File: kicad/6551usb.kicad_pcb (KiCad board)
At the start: 2 copper layers, 98.6 x 151.8 mm, 42 parts, among them J1 Conn_01x03_Male, P1 DLP-USB245R, SW1 SW_DIP_x06, U1 74LS04, U10 74LS74, U11 74LS86, U12 74LS33, U13 74LS273, U14 74LS374, U15 74LS244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

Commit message: Updated to 1.06
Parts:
- removed R4: 4.7k, Resistor_THT:R_Axial_DIN0207_L6.3mm_D2.5mm_P7.62mm_Horizontal
- moved R2 1.80 mm to (34.0, 126.9)
- moved R3 1.80 mm to (26.4, 132.0)
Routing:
- net /D5: track 176.3 -> 231.9 mm, vias 1 -> 0
- net /D3: track 190.2 -> 241.4 mm, vias 1 -> 2
- net /CD2: track 67.9 -> 119.0 mm, vias 1 -> 2
- net /D7: track 153.1 -> 203.5 mm, vias 0 -> 5
- net /E: track 131.7 -> 83.2 mm
- net /D1: track 190.7 -> 235.3 mm
- net /CTS*: track 83.0 -> 43.7 mm, vias 0 -> 2
- net /D6: track 173.3 -> 206.7 mm, vias 1 -> 6
- net /A7: track 98.9 -> 123.4 mm
- net /CART*: track 130.4 -> 151.6 mm, vias 0 -> 1
- net Net-(SW1-Pad12): track 28.0 -> 49.0 mm, vias 1 -> 0
- net GND: track 683.0 -> 702.8 mm, vias 0 -> 3
- net /A12: track 74.4 -> 91.2 mm
- net +5V: track 463.4 -> 480.2 mm
- net /R/W*: track 144.1 -> 160.2 mm, vias 1 -> 2
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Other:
- board text added: "USB Serial Pak for Color Computer v1.06 Copyright 2022 Don Barber License GPLv3 https://github.com/barberd/cocousbserial"
- board text removed: "USB Serial Pak for Color Computer v1.05 Copyright 2022 Don Barber License GPLv3 https://github.com/barberd/cocousbserial"

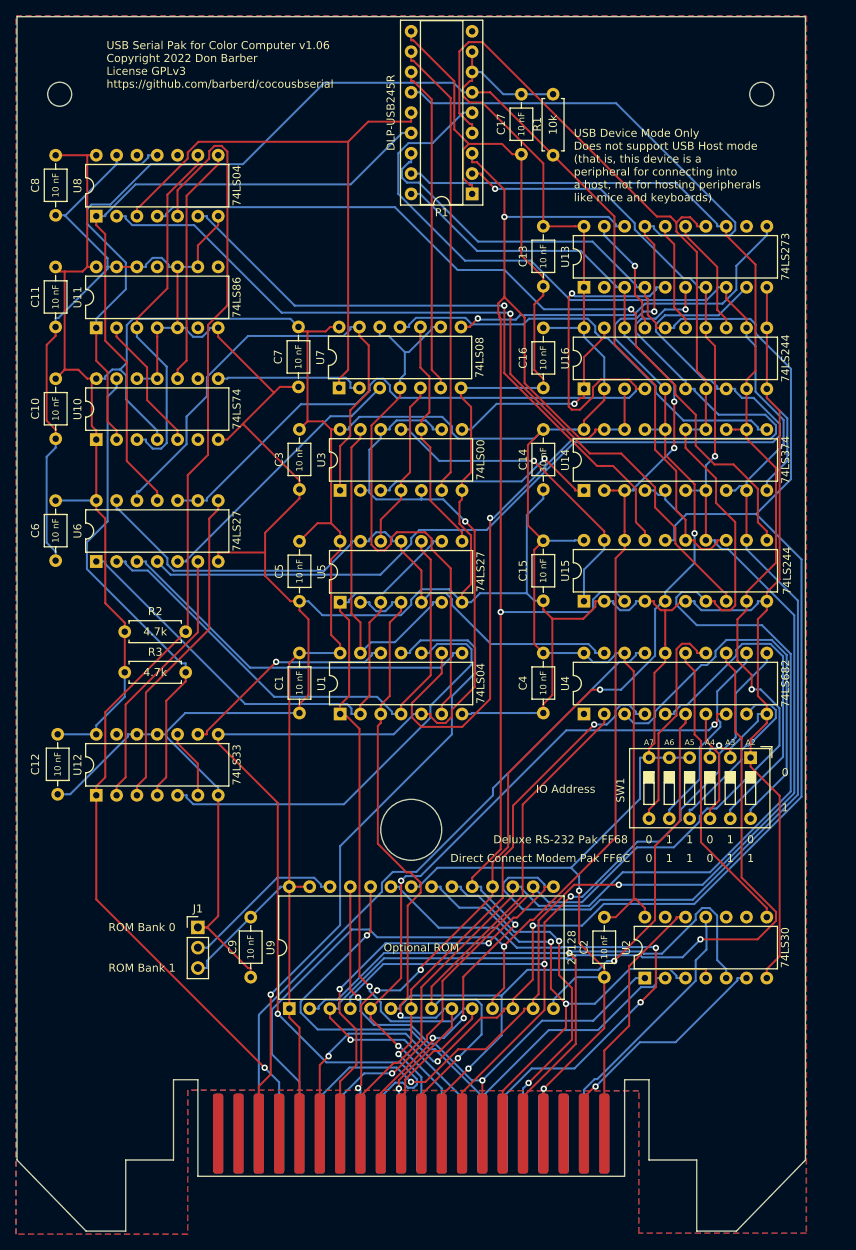
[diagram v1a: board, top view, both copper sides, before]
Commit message: Updated ears size for 1.07
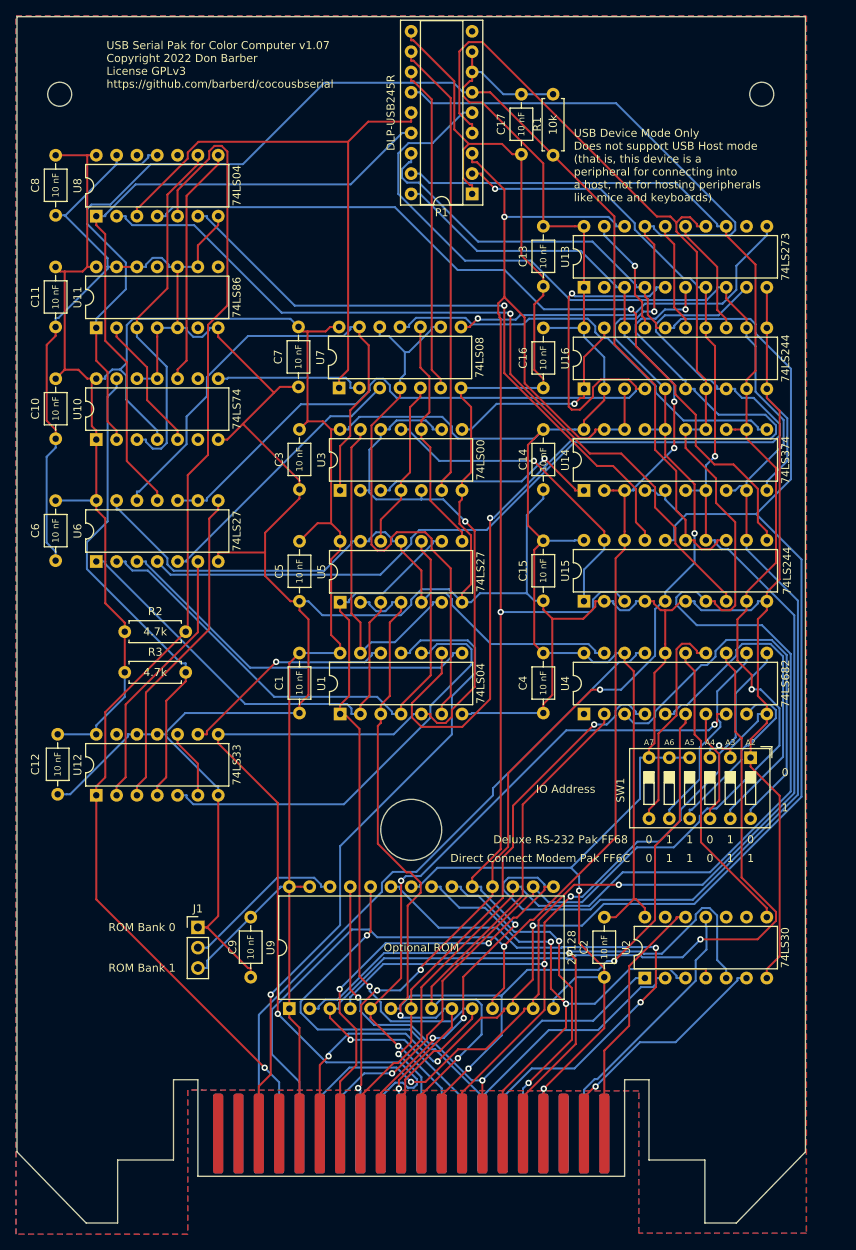
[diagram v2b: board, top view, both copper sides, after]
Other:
- board size 98.6 x 151.8 mm -> 98.6 x 150.8 mm
- board text added: "USB Serial Pak for Color Computer v1.07 Copyright 2022 Don Barber License GPLv3 https://github.com/barberd/cocousbserial"
- board text removed: "USB Serial Pak for Color Computer v1.06 Copyright 2022 Don Barber License GPLv3 https://github.com/barberd/cocousbserial"
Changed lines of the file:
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@@
   (title_block
     (title "CoCo USB Serial")
-    (date "2022-12-19")
-    (rev "1.06")
+    (date "2022-12-24")
+    (rev "1.07")
   )
   (layers
@@
   (gr_rect (start 18.415 58.42) (end 18.415 58.42) (layer "F.Mask") (width 0.15) (fill none))
   (gr_rect (start 91.948 192.913) (end 97.917 184.404) (layer "F.Mask") (width 0.15) (fill solid))
-  (gr_line (start 26.543 192.913) (end 32.512 192.913) (layer "Edge.Cuts") (width 0.1))
+  (gr_line (start 25.527 192.913) (end 32.512 192.913) (layer "Edge.Cuts") (width 0.1))
   (gr_line (start 88.9 182.88) (end 91.948 182.88) (layer "Edge.Cuts") (width 0.1))
   (gr_circle (center 106.045 59.69) (end 107.545 59.69) (layer "Edge.Cuts") (width 0.1) (fill none))
   (gr_line (start 35.56 182.88) (end 35.56 194.945) (layer "Edge.Cuts") (width 0.1))
-  (gr_line (start 26.543 192.913) (end 26.543 201.803) (layer "Edge.Cuts") (width 0.1))
+  (gr_line (start 25.527 192.913) (end 25.527 200.787) (layer "Edge.Cuts") (width 0.1))
   (gr_circle (center 60.96 132.08) (end 60.96 132.08) (layer "Edge.Cuts") (width 0.1) (fill none))
   (gr_line (start 35.56 194.945) (end 88.9 194.945) (layer "Edge.Cuts") (width 0.1))
-  (gr_line (start 12.954 192.913) (end 21.59 201.803) (layer "Edge.Cuts") (width 0.1))
+  (gr_line (start 12.954 191.897) (end 21.59 200.787) (layer "Edge.Cuts") (width 0.1))
   (gr_line (start 91.948 192.913) (end 91.948 182.88) (layer "Edge.Cuts") (width 0.1))
   (gr_line (start 88.9 182.88) (end 88.9 194.945) (layer "Edge.Cuts") (width 0.1))
   (gr_circle (center 18.288 59.69) (end 19.788 59.69) (layer "Edge.Cuts") (width 0.1) (fill none))
-  (gr_line (start 91.948 192.913) (end 97.917 192.913) (layer "Edge.Cuts") (width 0.1))
+  (gr_line (start 91.948 192.913) (end 98.933 192.913) (layer "Edge.Cuts") (width 0.1))
   (gr_circle (center 62.23 151.638) (end 66.04 151.638) (layer "Edge.Cuts") (width 0.1) (fill none))
-  (gr_line (start 97.917 201.803) (end 102.87 201.803) (layer "Edge.Cuts") (width 0.1))
+  (gr_line (start 98.933 200.787) (end 102.87 200.787) (layer "Edge.Cuts") (width 0.1))
   (gr_line (start 12.954 50) (end 111.506 50) (layer "Edge.Cuts") (width 0.1))
-  (gr_line (start 111.506 50) (end 111.506 192.913) (layer "Edge.Cuts") (width 0.1))
-  (gr_line (start 21.59 201.803) (end 26.543 201.803) (layer "Edge.Cuts") (width 0.1))
-  (gr_line (start 102.87 201.803) (end 111.506 192.913) (layer "Edge.Cuts") (width 0.1))
-  (gr_line (start 97.917 192.913) (end 97.917 201.803) (layer "Edge.Cuts") (width 0.1))
+  (gr_line (start 111.506 50) (end 111.506 191.897) (layer "Edge.Cuts") (width 0.1))
+  (gr_line (start 21.59 200.787) (end 25.527 200.787) (layer "Edge.Cuts") (width 0.1))
+  (gr_line (start 102.87 200.787) (end 111.506 191.897) (layer "Edge.Cuts") (width 0.1))
+  (gr_line (start 98.933 192.913) (end 98.933 200.787) (layer "Edge.Cuts") (width 0.1))
   (gr_line (start 32.512 182.88) (end 35.56 182.88) (layer "Edge.Cuts") (width 0.1))
-  (gr_line (start 12.954 192.913) (end 12.954 50) (layer "Edge.Cuts") (width 0.1))
+  (gr_line (start 12.954 191.897) (end 12.954 50) (layer "Edge.Cuts") (width 0.1))
   (gr_line (start 32.512 192.913) (end 32.512 182.88) (layer "Edge.Cuts") (width 0.1))
   (gr_text "0" (at 99.568 155.194) (layer "F.SilkS")
@@
     (effects (font (size 1 1) (thickness 0.15)))
   )
-  (gr_text "USB Serial Pak for Color Computer v1.06\nCopyright 2022 Don Barber\nLicense GPLv3\nhttps://github.com/barberd/cocousbserial" (at 24.13 56) (layer "F.SilkS")
+  (gr_text "USB Serial Pak for Color Computer v1.07\nCopyright 2022 Don Barber\nLicense GPLv3\nhttps://github.com/barberd/cocousbserial" (at 24.13 56) (layer "F.SilkS")
     (effects (font (size 1 1) (thickness 0.25)) (justify left))
   )

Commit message: v1.08: Updated to .1uf capacitors and slimmed width of card slightly
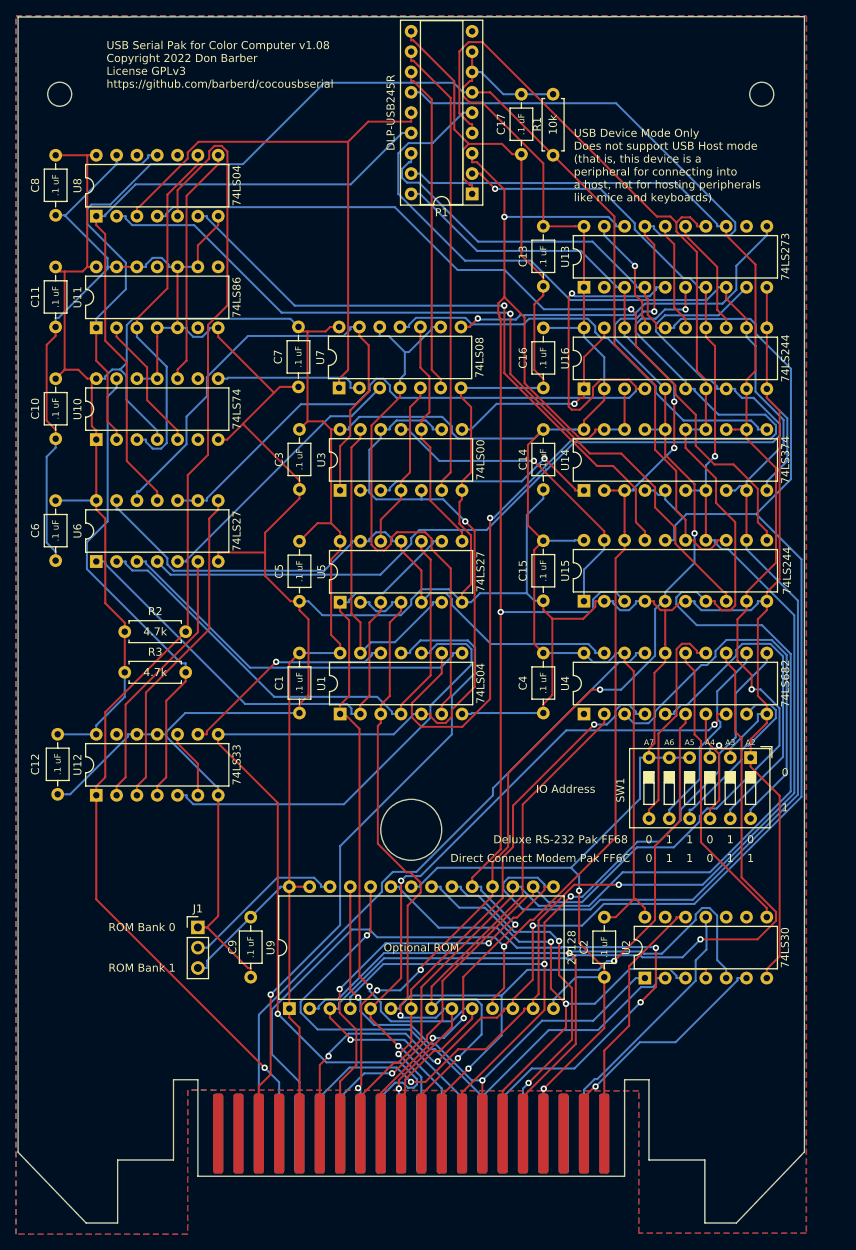
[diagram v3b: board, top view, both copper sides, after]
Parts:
- C1, C10, C11, C12, C13, C14, C15, C16, C17, C2, C3, C4, C5, C6, C7, C8, C9: value 10 nF -> .1 uF
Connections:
- U1 pad 12: Net-(U1-Pad12) -> unconnected-(U1-Pad12)
- U1 pad 13: /STATUS_SELECT -> GND
- U12 pad 10: /STATUS_WRITE -> unconnected-(U12-Pad10)
- U12 pad 6: /STATUS_WRITE -> /STATUS_SELECT
- U12 pad 8: /R/W* -> GND
- U12 pad 9: Net-(U1-Pad12) -> GND
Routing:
- net GND: track 702.8 -> 730.4 mm, vias 3 -> 4
- net Net-(U1-Pad12): track 27.5 -> 0.00 mm, vias 1 -> 0
- net /STATUS_WRITE: track 8.67 -> 0.00 mm
- net /STATUS_SELECT: track 41.8 -> 50.5 mm
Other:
- board size 98.6 x 150.8 mm -> 98.3 x 150.8 mm
- board text added: "USB Serial Pak for Color Computer v1.08 Copyright 2022 Don Barber License GPLv3 https://github.com/barberd/cocousbserial"
- board text removed: "USB Serial Pak for Color Computer v1.07 Copyright 2022 Don Barber License GPLv3 https://github.com/barberd/cocousbserial"

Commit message: Updated to version 1.09 with usb module power jumper
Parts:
- removed REF**: WEEE-Logo_5.6x8mm_SilkScreen, Symbol:WEEE-Logo_5.6x8mm_SilkScreen
- added JP1: Module Power, Connector_PinHeader_2.54mm:PinHeader_1x03_P2.54mm_Vertical, F.Cu at (77.7, 55.9)
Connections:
- P1 pad 7: +5V -> Net-(JP1-Pad2)
- P1 pad 9: unconnected-(P1-Pad9) -> Net-(JP1-Pad1)
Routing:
- net GND: track 730.4 -> 702.8 mm, vias 4 -> 3
- net unconnected-(U1-Pad12): track 0.00 -> 27.5 mm, vias 0 -> 1
- net Net-(JP1-Pad2): track 0.00 -> 11.5 mm
- net Net-(JP1-Pad1): track 0.00 -> 9.58 mm
- net unconnected-(U12-Pad10): track 0.00 -> 8.67 mm
- net /STATUS_SELECT: track 50.5 -> 41.8 mm
- net +5V: track 480.2 -> 479.1 mm, vias 0 -> 2
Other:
- board text added: "CoCo"
- board text added: "USB Host"
- board text added: "USB Serial Pak for Color Computer v1.09 Copyright 2023 Don Barber License GPLv3 https://github.com/barberd/cocousbserial"
- board text removed: "USB Serial Pak for Color Computer v1.08 Copyright 2022 Don Barber License GPLv3 https://github.com/barberd/cocousbserial"

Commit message: Fixed J2 label
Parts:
- removed JP1: Module Power, Connector_PinHeader_2.54mm:PinHeader_1x03_P2.54mm_Vertical
- added J2: Module Power, Connector_PinHeader_2.54mm:PinHeader_1x03_P2.54mm_Vertical, F.Cu at (82.8, 55.9)
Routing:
- net GND: track 702.8 -> 730.4 mm, vias 3 -> 4
- net unconnected-(U1-Pad12): track 27.5 -> 0.00 mm, vias 1 -> 0
